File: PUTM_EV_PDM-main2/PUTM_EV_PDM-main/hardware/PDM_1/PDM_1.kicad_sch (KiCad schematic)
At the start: 6 parts, among them U1 STM32G0C1KCTxN

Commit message: lepsze footprinty
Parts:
- FB1: footprint (none) -> Resistor_SMD:R_0603_1608Metric_Pad0.98x0.95mm_HandSolder
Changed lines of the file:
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@@
       (effects (font (size 1.27 1.27)))
     )
-    (property "Footprint" "" (at 184.15 37.338 90)
+    (property "Footprint" "Resistor_SMD:R_0603_1608Metric_Pad0.98x0.95mm_HandSolder" (at 184.15 37.338 90)
       (effects (font (size 1.27 1.27)) hide)
     )
-    (property "Datasheet" "~" (at 184.15 35.56 0)
+    (property "Datasheet" "https://www.mouser.pl/ProductDetail/Murata-Electronics/BLM18SP102SZ1D?qs=W%2FMpXkg%252BdQ7HBmR7E%252BlIwg%3D%3D" (at 184.15 35.56 0)
       (effects (font (size 1.27 1.27)) hide)
     )

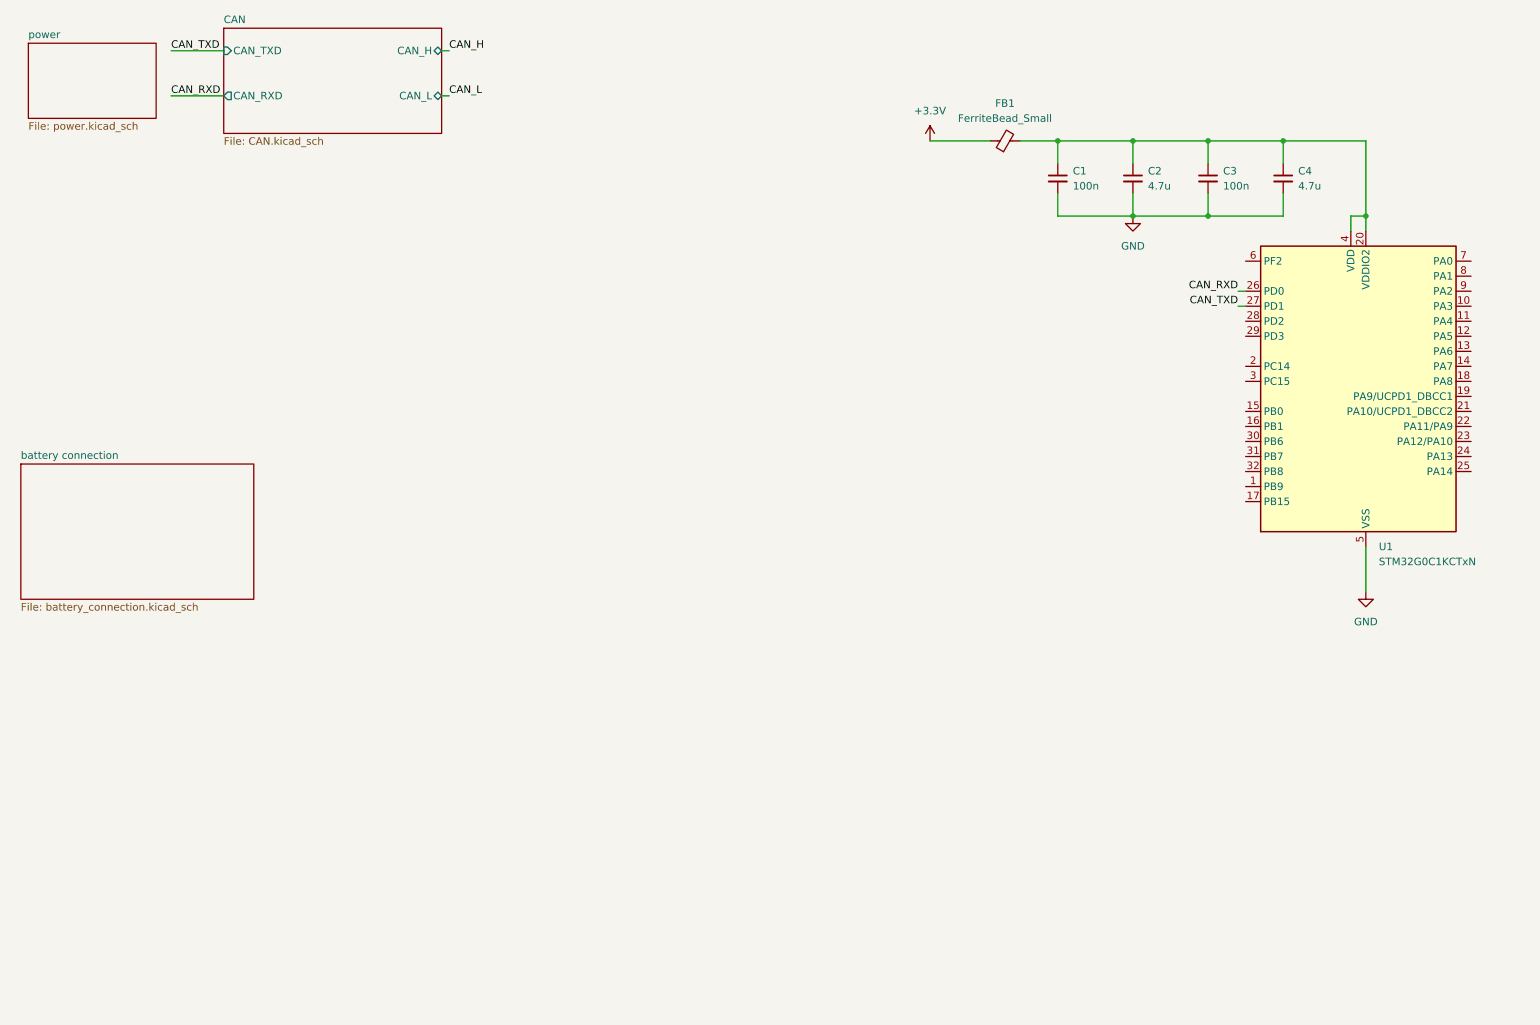
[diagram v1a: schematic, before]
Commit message: nowe połączenia
dodane połączenia z STM
dodane złącza
dodane LED
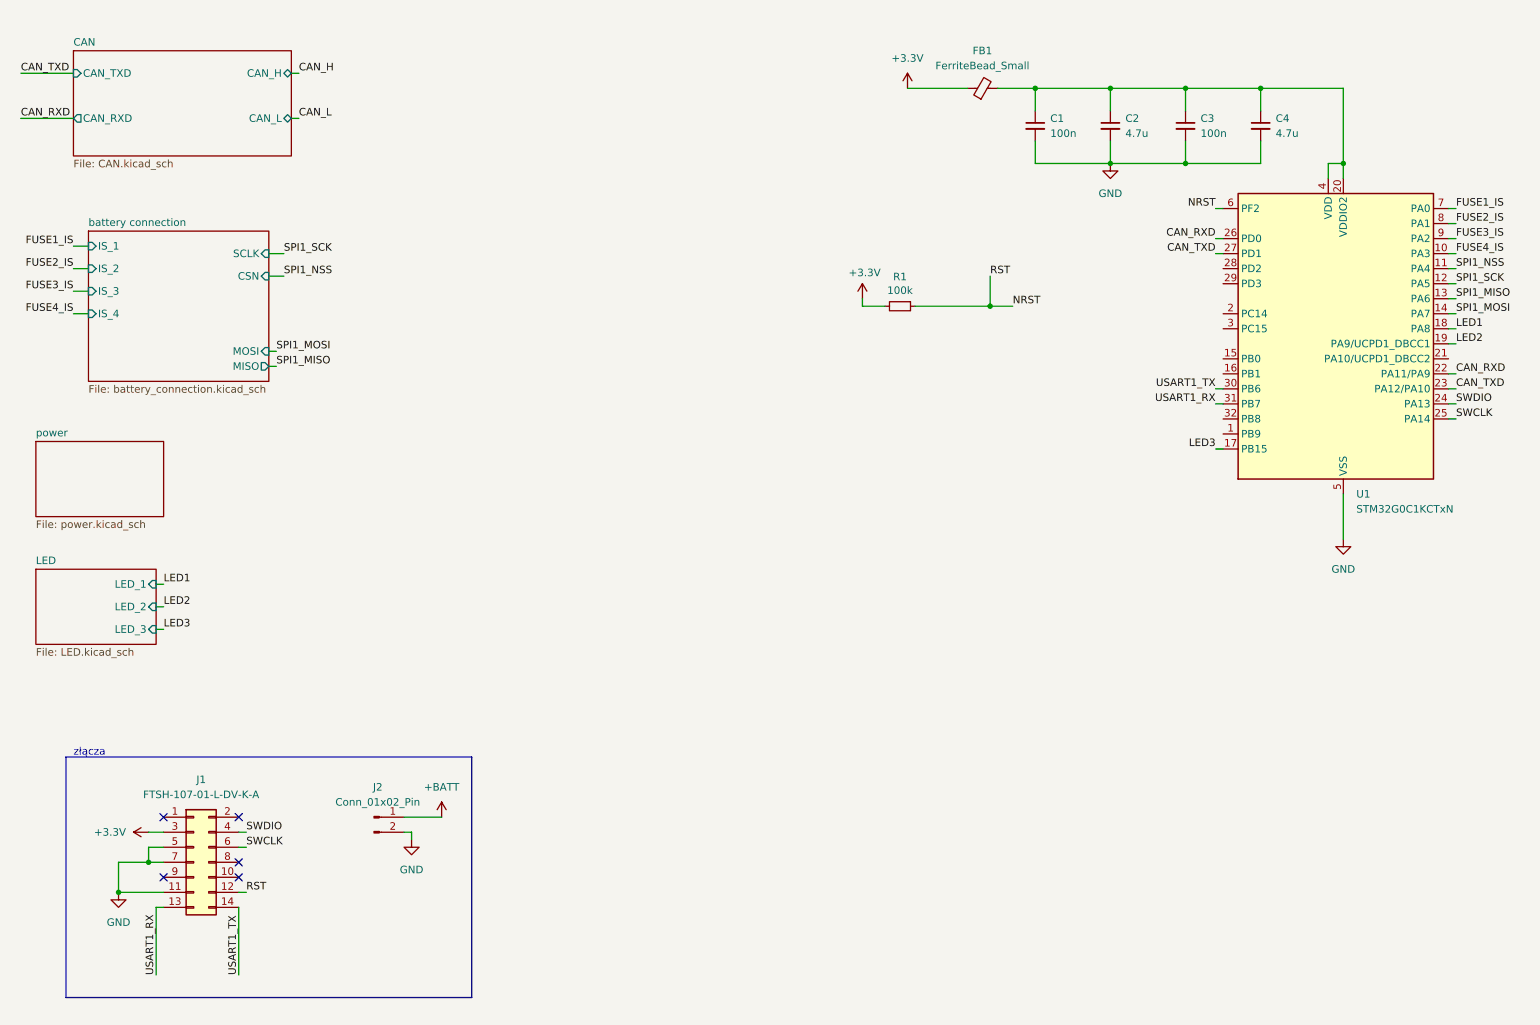
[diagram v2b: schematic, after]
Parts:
- added J1: FTSH-107-01-L-DV-K-A, Samacsys:FTSH-107-XX-YYY-DV-K-A, symbol ftsh-107-01-l-dv-k-a:FTSH-107-01-L-DV-K-A
- added J2: Conn_01x02_Pin, Connector_Wire:SolderWire-0.75sqmm_1x02_P7mm_D1.25mm_OD3.5mm_Relief, symbol Connector:Conn_01x02_Pin
- added R1: 100k, Resistor_SMD:R_0603_1608Metric, symbol Device:R_Small
- FB1: footprint Resistor_SMD:R_0603_1608Metric_Pad0.98x0.95mm_HandSolder -> Inductor_SMD:L_0603_1608Metric
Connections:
- net +3.3V: now also J1.3 (Pin_3)
- net CAN_RXD: now also U1.22 (PA11/PA9)
- net CAN_TXD: now also U1.23 (PA12/PA10)
- net GND: now also J1.11 (Pin_11), J1.5 (Pin_5), J1.7 (Pin_7), J2.2 (Pin_2)
- net FUSE4_IS: now reaches U1.10 (PA3)
- net SPI1_NSS: now reaches U1.11 (PA4)
- net SPI1_SCK: now reaches U1.12 (PA5)
- net SPI1_MISO: now reaches U1.13 (PA6)
- net SPI1_MOSI: now reaches U1.14 (PA7)
- net LED3: now reaches U1.17 (PB15)
- net LED1: now reaches U1.18 (PA8)
- net LED2: now reaches U1.19 (PA9/UCPD1_DBCC1)
- net SWDIO: now reaches U1.24 (PA13)
- net SWDIO: now also J1.4 (Pin_4)
- net SWCLK: now reaches U1.25 (PA14)
- net SWCLK: now also J1.6 (Pin_6)
- net USART1_TX: now reaches U1.30 (PB6)
- net USART1_TX: now also J1.14 (Pin_14)
- net USART1_RX: now reaches U1.31 (PB7)
- net USART1_RX: now also J1.13 (Pin_13)
- net NRST: now reaches U1.6 (PF2)
- net NRST: now also J1.12 (Pin_12), R1.1
- net FUSE1_IS: now reaches U1.7 (PA0)
- net FUSE2_IS: now reaches U1.8 (PA1)
- net FUSE3_IS: now reaches U1.9 (PA2)
- new net +3V3: R1.2
- new net +BATT: J2.1 (Pin_1)
- no-connect marks 0 -> 5
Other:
- added sheet LED (LED.kicad_sch)
- sheet battery connection ports: added CSN, IS_1, IS_2, IS_3, IS_4, MISO, MOSI, SCLK; removed none
- note added: "złącza"
- moved on the sheet: C1, C2, C3, C4, FB1, U1

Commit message: małe zmiany
dodano złącza
zmieniono parę footprintów
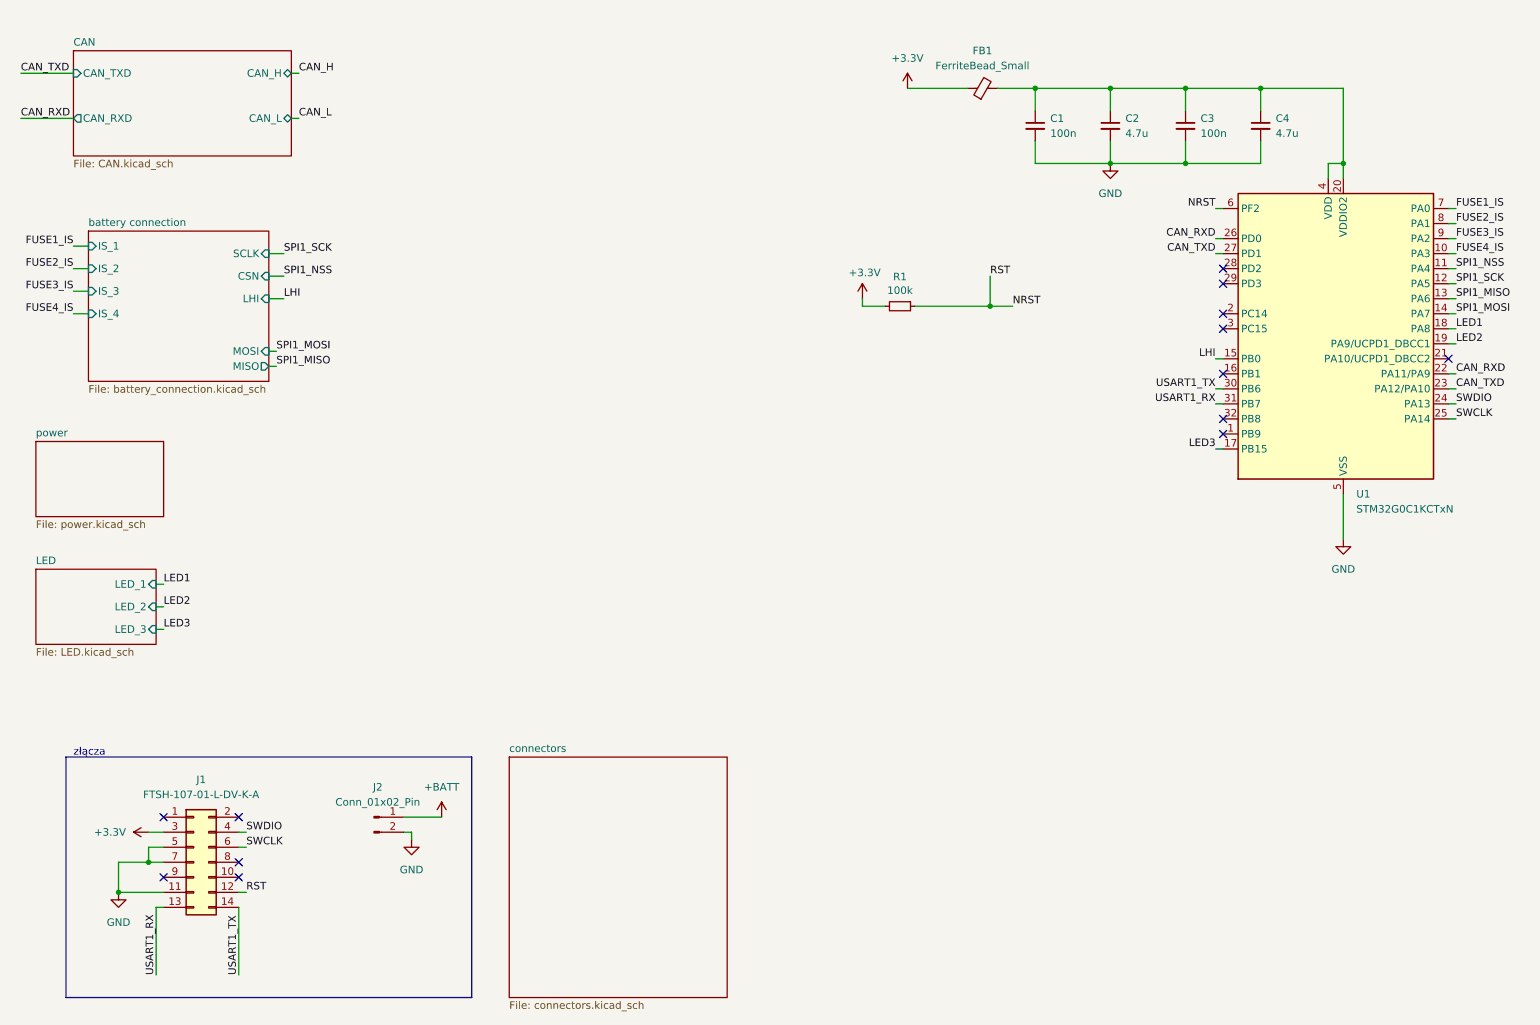
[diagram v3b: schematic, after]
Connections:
- net LHI: now reaches U1.15 (PB0)
- no-connect marks 5 -> 13
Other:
- added sheet connectors (connectors.kicad_sch)
- sheet battery connection ports: added LHI; removed none
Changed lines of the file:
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@@
   )
   (no_connect (at 54.61 149.86))
+  (no_connect (at 220.98 74.93))
+  (no_connect (at 220.98 85.09))
   (no_connect (at 41.91 149.86))
+  (no_connect (at 220.98 57.15))
+  (no_connect (at 259.08 72.39))
+  (no_connect (at 220.98 59.69))
   (no_connect (at 54.61 157.48))
   (no_connect (at 41.91 160.02))
+  (no_connect (at 220.98 67.31))
+  (no_connect (at 220.98 64.77))
+  (no_connect (at 220.98 82.55))
   (no_connect (at 54.61 160.02))
   (wire (pts (xy 39.37 152.4) (xy 41.91 152.4))
@@
     (stroke (width 0) (type default))
   )
+  (wire (pts (xy 59.69 62.23) (xy 62.23 62.23))
+    (stroke (width 0) (type default))
+  )
   (wire (pts (xy 59.69 58.42) (xy 62.23 58.42))
     (stroke (width 0) (type default))
@@
   )
   (wire (pts (xy 189.23 26.67) (xy 201.93 26.67))
+    (stroke (width 0) (type default))
+  )
+  (wire (pts (xy 219.71 72.39) (xy 220.98 72.39))
     (stroke (width 0) (type default))
   )
@@
     (effects (font (size 1.27 1.27)) (justify left bottom))
   )
+  (label "LHI" (at 62.23 62.23 0) (fields_autoplaced)
+    (effects (font (size 1.27 1.27)) (justify left bottom))
+  )
   (label "SWDIO" (at 55.88 152.4 0) (fields_autoplaced)
     (effects (font (size 1.27 1.27)) (justify left bottom))
@@
   )
   (label "FUSE2_IS" (at 26.67 57.15 180) (fields_autoplaced)
+    (effects (font (size 1.27 1.27)) (justify right bottom))
+  )
+  (label "LHI" (at 219.71 72.39 180) (fields_autoplaced)
     (effects (font (size 1.27 1.27)) (justify right bottom))
   )
@@
     )
   )
+  (sheet (at 100.33 139.7) (size 36.83 40.64) (fields_autoplaced)
+    (stroke (width 0.1524) (type solid))
+    (fill (color 0 0 0 0.0000))
+    (property "Sheetname" "connectors" (at 100.33 138.9884 0)
+      (effects (font (size 1.27 1.27)) (justify left bottom))
+    )
+    (property "Sheetfile" "connectors.kicad_sch" (at 100.33 180.9246 0)
+      (effects (font (size 1.27 1.27)) (justify left top))
+    )
+    (instances
+      (project "PDM_1"
+        (path "/b652b05a-4e3d-4ad1-b032-18886abe7d45" (page "10"))
+      )
+    )
+  )
   (sheet (at 26.67 20.32) (size 36.83 17.78) (fields_autoplaced)
     (stroke (width 0.1524) (type solid))
@@
       (effects (font (size 1.27 1.27)) (justify left))
     )
-    (instances
+    (pin "LHI" input (at 59.69 62.23 0)
+      (effects (font (size 1.27 1.27)) (justify right))
+    )
+    (instances

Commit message: piny na płytce
Dodano ułożenie pinów na płytce
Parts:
- removed J2: Conn_01x02_Pin, Connector_Wire:SolderWire-0.75sqmm_1x02_P7mm_D1.25mm_OD3.5mm_Relief, symbol Connector:Conn_01x02_Pin
- J1: footprint Samacsys:FTSH-107-XX-YYY-DV-K-A -> FTSH-107-01-L-DV-K-A:FTSH-107-XX-YYY-DV-K-A
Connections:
- net LHI_4: now reaches U1.16 (PB1)
- net LHI_1: now reaches U1.28 (PD2)
- net LHI_2: now reaches U1.29 (PD3)
- net LHI renamed LHI_3
- no-connect marks 13 -> 10
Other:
- sheet battery connection ports: added LHI_1, LHI_2, LHI_3, LHI_4; removed LHI
